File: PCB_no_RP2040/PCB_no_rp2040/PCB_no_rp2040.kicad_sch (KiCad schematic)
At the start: 19 parts, among them J1 Conn_02x16_Counter_Clockwise, J2 Conn_02x16_Counter_Clockwise, J3 Conn_02x16_Counter_Clockwise, U1 74HC595, U2 74HC595, U3 74HC595, U4 74HC595, U5 74HC595, U6 74HC595, U7 74HC595, U8 MAX11643EEG, U9 MAX11643EEG

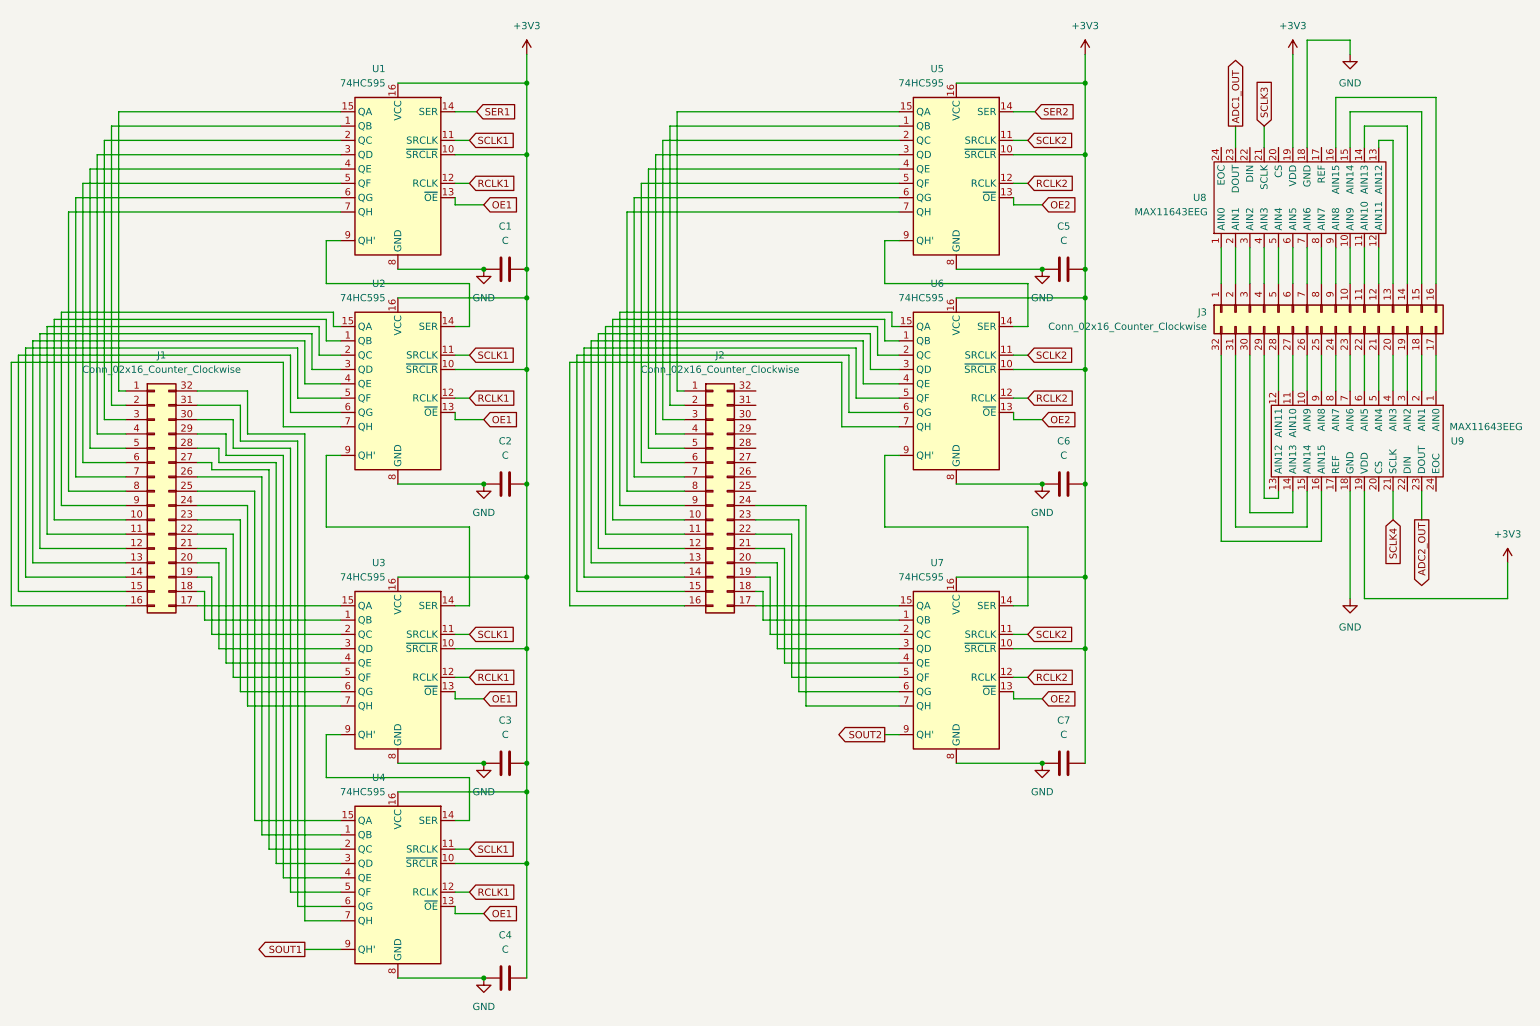
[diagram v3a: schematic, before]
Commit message: Changed all shift registers to be on the same SCLK, RCLK and OE. Also connected shift register 4 to 5 using node names
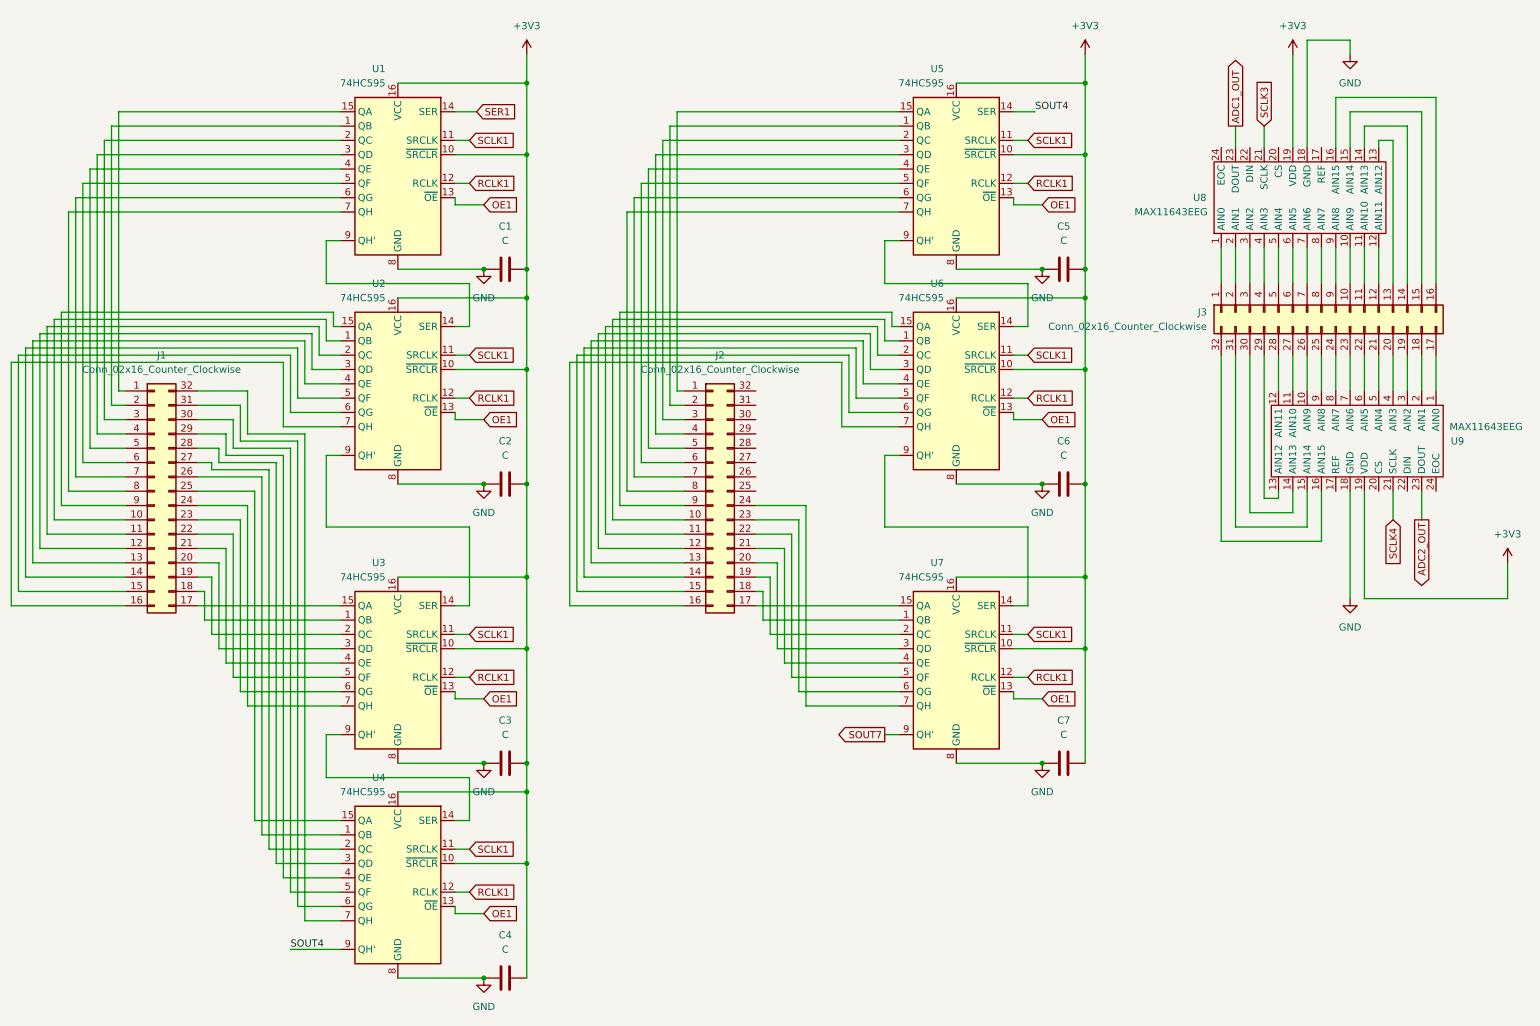
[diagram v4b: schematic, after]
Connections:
- net OE2 is gone; now on net OE1: U5.13 (~{OE}), U6.13 (~{OE}), U7.13 (~{OE})
- net RCLK2 is gone; now on net RCLK1: U5.12 (RCLK), U6.12 (RCLK), U7.12 (RCLK)
- net SCLK2 is gone; now on net SCLK1: U5.11 (SRCLK), U6.11 (SRCLK), U7.11 (SRCLK)
- net SOUT1 is gone; now on net SOUT4: U4.9 (QH')
- net SER2 renamed SOUT4
- net SOUT2 renamed SOUT7

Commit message: Turned all shift register outputs into nodes to make schematic cleaner and replaced old connectors w the actual 30x2 connector
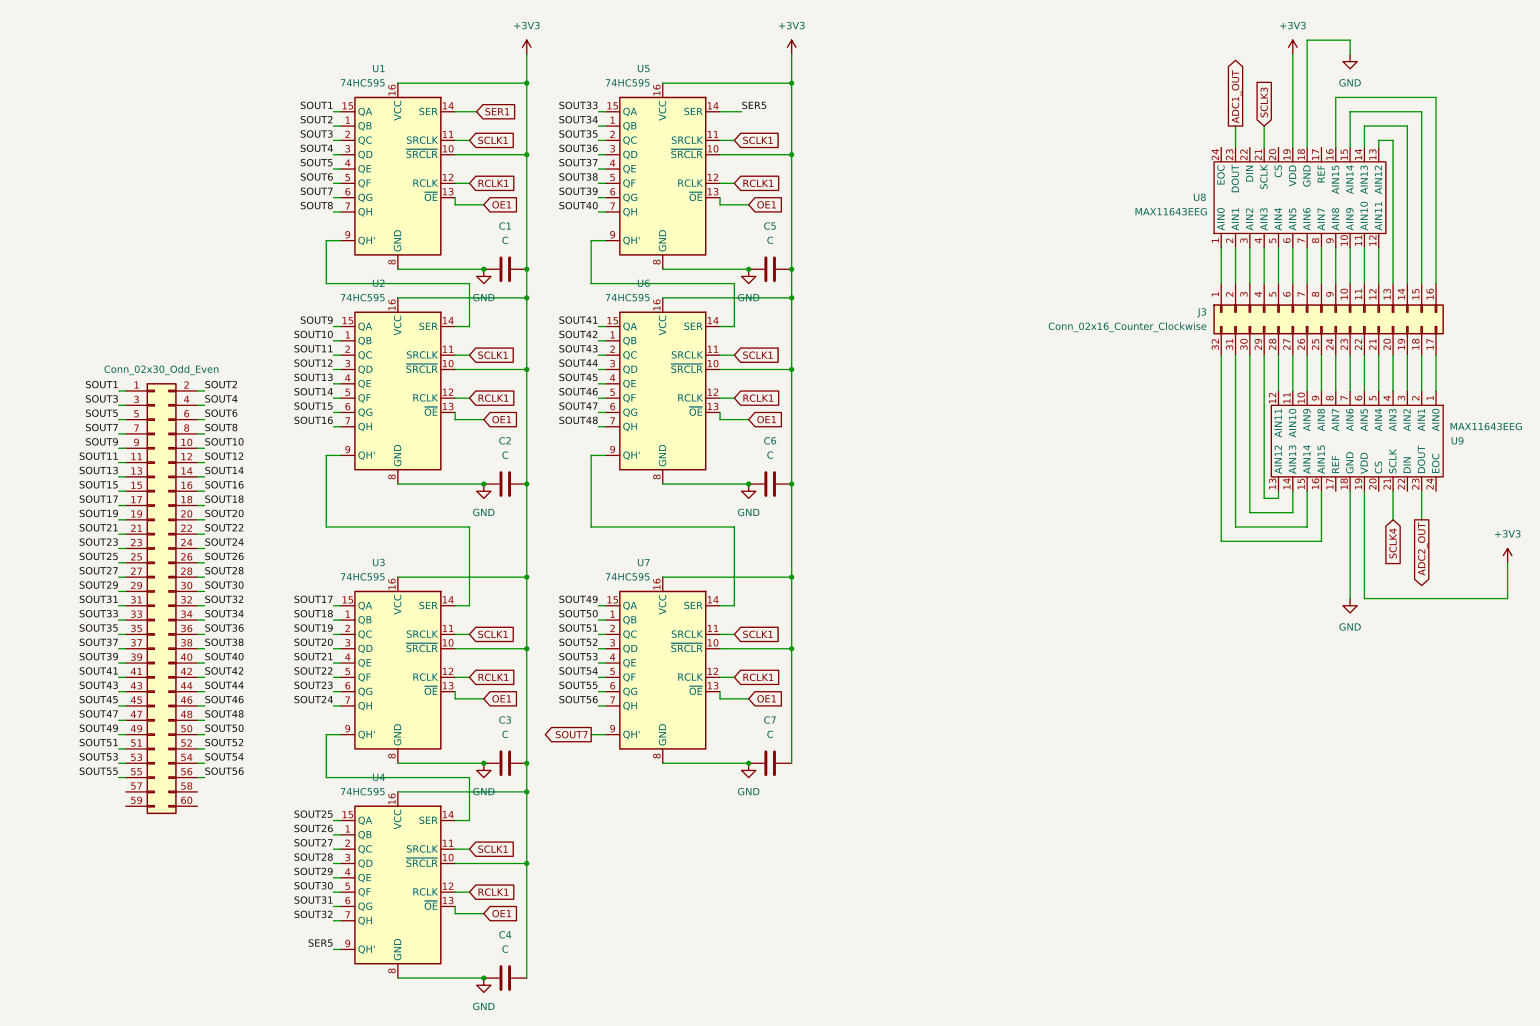
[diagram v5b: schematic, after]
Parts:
- removed J1, J2: Conn_02x16_Counter_Clockwise, symbol Connector_Generic:Conn_02x16_Counter_Clockwise
- added J1: Conn_02x30_Odd_Even, symbol Connector_Generic:Conn_02x30_Odd_Even
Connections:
- net SOUT4: now also U1.3 (QD), J1.4 (Pin_4); no longer U4.9 (QH'), U5.14 (SER)
- net SOUT7: now also U1.6 (QG), J1.7 (Pin_7)
- net SOUT1: now reaches U1.15 (QA)
- net SOUT1: now also J1.1 (Pin_1)
- net SOUT10: now reaches U2.1 (QB)
- net SOUT10: now also J1.10 (Pin_10)
- net SOUT11: now reaches U2.2 (QC)
- net SOUT11: now also J1.11 (Pin_11)
- net SOUT12: now reaches U2.3 (QD)
- net SOUT12: now also J1.12 (Pin_12)
- net SOUT13: now reaches U2.4 (QE)
- net SOUT13: now also J1.13 (Pin_13)
- net SOUT14: now reaches U2.5 (QF)
- net SOUT14: now also J1.14 (Pin_14)
- net SOUT15: now reaches U2.6 (QG)
- net SOUT15: now also J1.15 (Pin_15)
- net SOUT16: now reaches U2.7 (QH)
- net SOUT16: now also J1.16 (Pin_16)
- net SOUT17: now reaches U3.15 (QA)
- net SOUT17: now also J1.17 (Pin_17)
- net SOUT18: now reaches U3.1 (QB)
- net SOUT18: now also J1.18 (Pin_18)
- net SOUT19: now reaches U3.2 (QC)
- net SOUT19: now also J1.19 (Pin_19)
- net SOUT2: now reaches U1.1 (QB)
- net SOUT2: now also J1.2 (Pin_2)
- net SOUT20: now reaches U3.3 (QD)
- net SOUT20: now also J1.20 (Pin_20)
- net SOUT21: now reaches U3.4 (QE)
- net SOUT21: now also J1.21 (Pin_21)
- net SOUT22: now reaches U3.5 (QF)
- net SOUT22: now also J1.22 (Pin_22)
- net SOUT23: now reaches U3.6 (QG)
- net SOUT23: now also J1.23 (Pin_23)
- net SOUT24: now reaches U3.7 (QH)
- net SOUT24: now also J1.24 (Pin_24)
- net SOUT25: now reaches U4.15 (QA)
- net SOUT25: now also J1.25 (Pin_25)
- net SOUT26: now reaches U4.1 (QB)
- net SOUT26: now also J1.26 (Pin_26)
- net SOUT27: now reaches U4.2 (QC)
- net SOUT27: now also J1.27 (Pin_27)
- net SOUT28: now reaches U4.3 (QD)
- net SOUT28: now also J1.28 (Pin_28)
- net SOUT29: now reaches U4.4 (QE)
- net SOUT29: now also J1.29 (Pin_29)
- net SOUT3: now reaches U1.2 (QC)
- net SOUT3: now also J1.3 (Pin_3)
- net SOUT30: now reaches U4.5 (QF)
- net SOUT30: now also J1.30 (Pin_30)
- net SOUT31: now reaches U4.6 (QG)
- net SOUT31: now also J1.31 (Pin_31)
- net SOUT32: now reaches U4.7 (QH)
- net SOUT32: now also J1.32 (Pin_32)
- net SOUT5: now reaches U1.4 (QE)
- net SOUT5: now also J1.5 (Pin_5)
- net SOUT6: now reaches U1.5 (QF)
- net SOUT6: now also J1.6 (Pin_6)
- net SOUT8: now reaches U1.7 (QH)
- net SOUT8: now also J1.8 (Pin_8)
- net SOUT9: now reaches U2.15 (QA)
- net SOUT9: now also J1.9 (Pin_9)
- net SOUT34: now reaches U5.1 (QB)
- net SOUT34: now also J1.34 (Pin_34)
- net SOUT33: now reaches U5.15 (QA)
- net SOUT33: now also J1.33 (Pin_33)
- net SOUT35: now reaches U5.2 (QC)
- net SOUT35: now also J1.35 (Pin_35)
- net SOUT36: now reaches U5.3 (QD)
- net SOUT36: now also J1.36 (Pin_36)
- net SOUT37: now reaches U5.4 (QE)
- net SOUT37: now also J1.37 (Pin_37)
- net SOUT38: now reaches U5.5 (QF)
- net SOUT38: now also J1.38 (Pin_38)
- net SOUT39: now reaches U5.6 (QG)
- net SOUT39: now also J1.39 (Pin_39)
- net SOUT40: now reaches U5.7 (QH)
- net SOUT40: now also J1.40 (Pin_40)
- net SOUT50: now reaches U7.1 (QB)
- net SOUT50: now also J1.50 (Pin_50)
- net SOUT49: now reaches U7.15 (QA)
- net SOUT49: now also J1.49 (Pin_49)
- net SOUT51: now reaches U7.2 (QC)
- net SOUT51: now also J1.51 (Pin_51)
- net SOUT52: now reaches U7.3 (QD)
- net SOUT52: now also J1.52 (Pin_52)
- net SOUT53: now reaches U7.4 (QE)
- net SOUT53: now also J1.53 (Pin_53)
- net SOUT54: now reaches U7.5 (QF)
- net SOUT54: now also J1.54 (Pin_54)
- net SOUT55: now reaches U7.6 (QG)
- net SOUT55: now also J1.55 (Pin_55)
- net SOUT56: now reaches U7.7 (QH)
- net SOUT56: now also J1.56 (Pin_56)
- net SOUT42: now reaches U6.1 (QB)
- net SOUT42: now also J1.42 (Pin_42)
- net SOUT43: now reaches U6.2 (QC)
- net SOUT43: now also J1.43 (Pin_43)
- net SOUT44: now reaches U6.3 (QD)
- net SOUT44: now also J1.44 (Pin_44)
- net SOUT45: now reaches U6.4 (QE)
- net SOUT45: now also J1.45 (Pin_45)
- net SOUT46: now reaches U6.5 (QF)
- net SOUT46: now also J1.46 (Pin_46)
- net SOUT47: now reaches U6.6 (QG)
- net SOUT47: now also J1.47 (Pin_47)
- net SOUT48: now reaches U6.7 (QH)
- net SOUT48: now also J1.48 (Pin_48)
- net SOUT41: now reaches U6.15 (QA)
- net SOUT41: now also J1.41 (Pin_41)
- new net SER5: U4.9 (QH'), U5.14 (SER)
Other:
- moved on the sheet: C5, C6, C7, U5, U6, U7

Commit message: used nodes to reconnect ADC's to new connectors and added voltage dividers to all ADC inputs
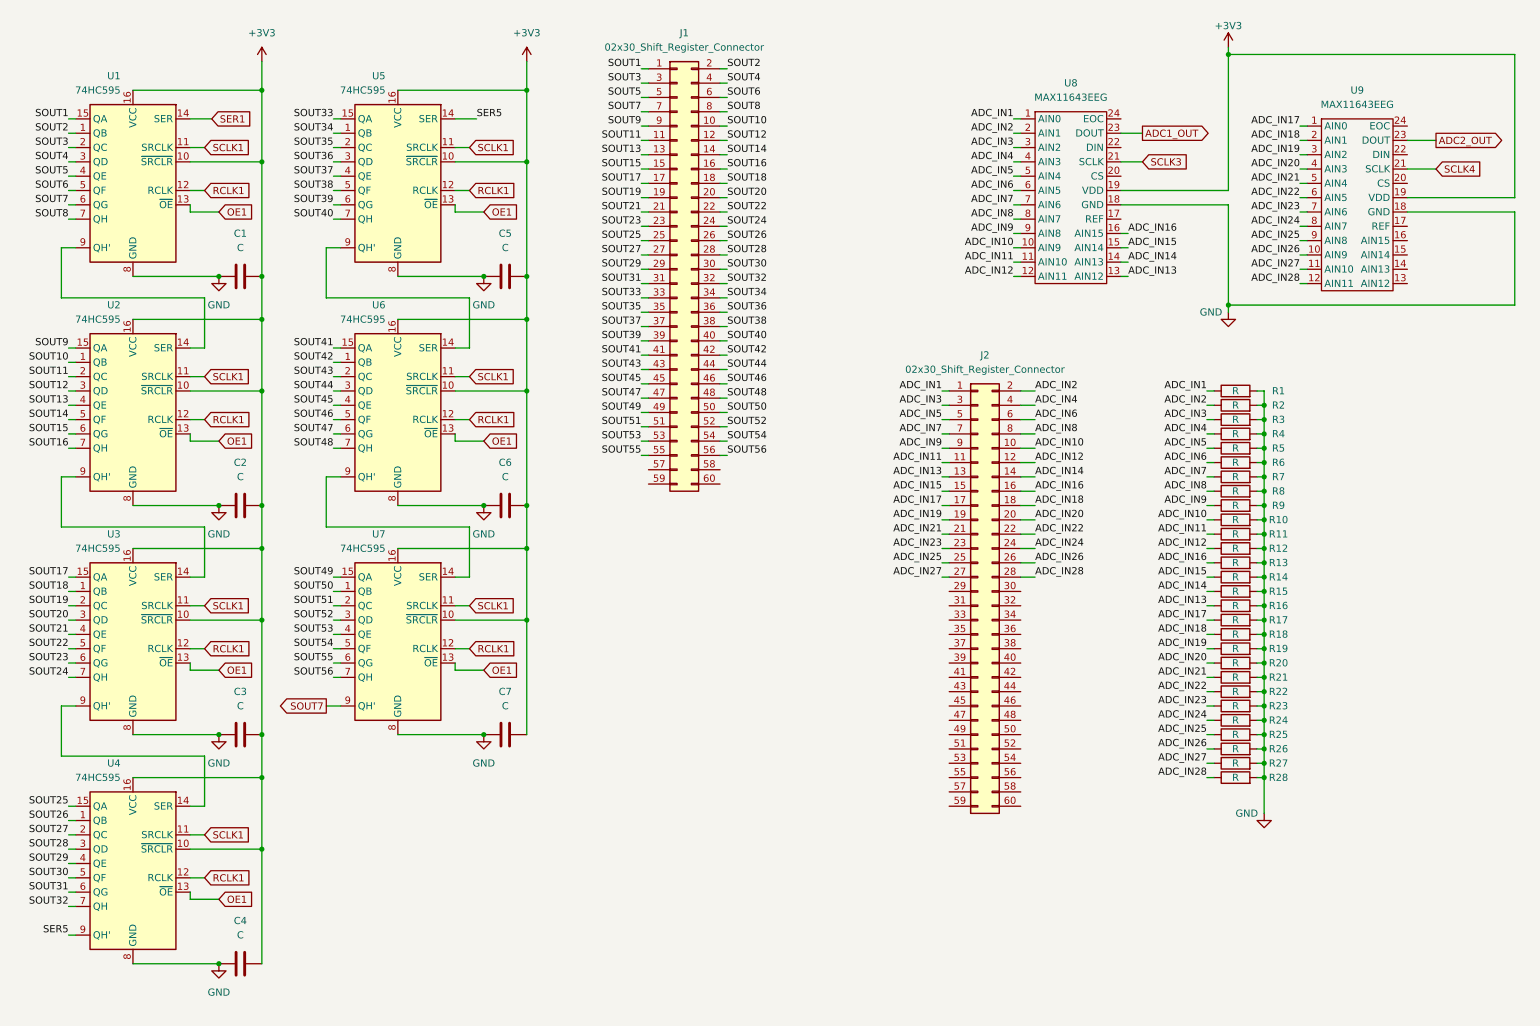
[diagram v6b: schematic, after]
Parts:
- removed J3: Conn_02x16_Counter_Clockwise, symbol Connector_Generic:Conn_02x16_Counter_Clockwise
- added J2: 02x30_Shift_Register_Connector, symbol Connector_Generic:Conn_02x30_Odd_Even
- added R1, R10, R11, R12, R13, R14, R15, R16, R17, R18, R19, R2, R20, R21, R22, R23, R24, R25, R26, R27, R28, R3, R4, R5, R6, R7, R8, R9: R, symbol Device:R
- J1: value Conn_02x30_Odd_Even -> 02x30_Shift_Register_Connector
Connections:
- net GND: now also R1.2, R10.2, R11.2, R12.2, R13.2, R14.2, R15.2, R16.2, R17.2, R18.2, R19.2, R2.2, R20.2, R21.2, R22.2, R23.2, R24.2, R25.2, R26.2, R27.2, R28.2, R3.2, R4.2, R5.2, R6.2, R7.2, R8.2, R9.2
- net ADC_IN1: now reaches U8.1 (AIN0)
- net ADC_IN1: now also J2.1 (Pin_1), R1.1
- net ADC_IN10: now reaches U8.10 (AIN9)
- net ADC_IN10: now also J2.10 (Pin_10), R10.1
- net ADC_IN11: now reaches U8.11 (AIN10)
- net ADC_IN11: now also J2.11 (Pin_11), R11.1
- net ADC_IN12: now reaches U8.12 (AIN11)
- net ADC_IN12: now also J2.12 (Pin_12), R12.1
- net ADC_IN13: now reaches U8.13 (AIN12)
- net ADC_IN13: now also J2.13 (Pin_13), R16.1
- net ADC_IN14: now reaches U8.14 (AIN13)
- net ADC_IN14: now also J2.14 (Pin_14), R15.1
- net ADC_IN15: now reaches U8.15 (AIN14)
- net ADC_IN15: now also J2.15 (Pin_15), R14.1
- net ADC_IN16: now reaches U8.16 (AIN15)
- net ADC_IN16: now also J2.16 (Pin_16), R13.1
- net ADC_IN17: now reaches U9.1 (AIN0)
- net ADC_IN17: now also J2.17 (Pin_17), R17.1
- net ADC_IN18: now reaches U9.2 (AIN1)
- net ADC_IN18: now also J2.18 (Pin_18), R18.1
- net ADC_IN19: now reaches U9.3 (AIN2)
- net ADC_IN19: now also J2.19 (Pin_19), R19.1
- net ADC_IN2: now reaches U8.2 (AIN1)
- net ADC_IN2: now also J2.2 (Pin_2), R2.1
- net ADC_IN20: now reaches U9.4 (AIN3)
- net ADC_IN20: now also J2.20 (Pin_20), R20.1
- net ADC_IN21: now reaches U9.5 (AIN4)
- net ADC_IN21: now also J2.21 (Pin_21), R21.1
- net ADC_IN22: now reaches U9.6 (AIN5)
- net ADC_IN22: now also J2.22 (Pin_22), R22.1
- net ADC_IN23: now reaches U9.7 (AIN6)
- net ADC_IN23: now also J2.23 (Pin_23), R23.1
- net ADC_IN24: now reaches U9.8 (AIN7)
- net ADC_IN24: now also J2.24 (Pin_24), R24.1
- net ADC_IN25: now reaches U9.9 (AIN8)
- net ADC_IN25: now also J2.25 (Pin_25), R25.1
- net ADC_IN26: now reaches U9.10 (AIN9)
- net ADC_IN26: now also J2.26 (Pin_26), R26.1
- net ADC_IN27: now reaches U9.11 (AIN10)
- net ADC_IN27: now also J2.27 (Pin_27), R27.1
- net ADC_IN28: now reaches U9.12 (AIN11)
- net ADC_IN28: now also J2.28 (Pin_28), R28.1
- net ADC_IN3: now reaches U8.3 (AIN2)
- net ADC_IN3: now also J2.3 (Pin_3), R3.1
- net ADC_IN4: now reaches U8.4 (AIN3)
- net ADC_IN4: now also J2.4 (Pin_4), R4.1
- net ADC_IN5: now reaches U8.5 (AIN4)
- net ADC_IN5: now also J2.5 (Pin_5), R5.1
- net ADC_IN6: now reaches U8.6 (AIN5)
- net ADC_IN6: now also J2.6 (Pin_6), R6.1
- net ADC_IN7: now reaches U8.7 (AIN6)
- net ADC_IN7: now also J2.7 (Pin_7), R7.1
- net ADC_IN8: now reaches U8.8 (AIN7)
- net ADC_IN8: now also J2.8 (Pin_8), R8.1
- net ADC_IN9: now reaches U8.9 (AIN8)
- net ADC_IN9: now also J2.9 (Pin_9), R9.1
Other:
- moved on the sheet: C1, C2, C3, C4, C5, C6, C7, U1, U2, U3, U4, U5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
